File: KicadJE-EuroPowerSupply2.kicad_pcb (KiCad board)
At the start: 2 copper layers, 159 x 128 mm, 148 parts, among them J101 RampOut1, J102 PulseOut2, J103 SawOut3, J104 In1.1, J105 In1.2, J106 In1.3, J107 SS_In2, J108 HS_In3, J109 FM_In4, J110 PWM_In5, J111 SineOut4, P101 HEADER_2x5_Doepfer, Q101 MMBT3906, Q102 UMX1N, SW101 Octave (3 state), U101 TL072, U102 TL072, U103 TL072, U104 AS3340, U105 L78L05_SOT89, U106 L79L05_SOT89, U107 TL072

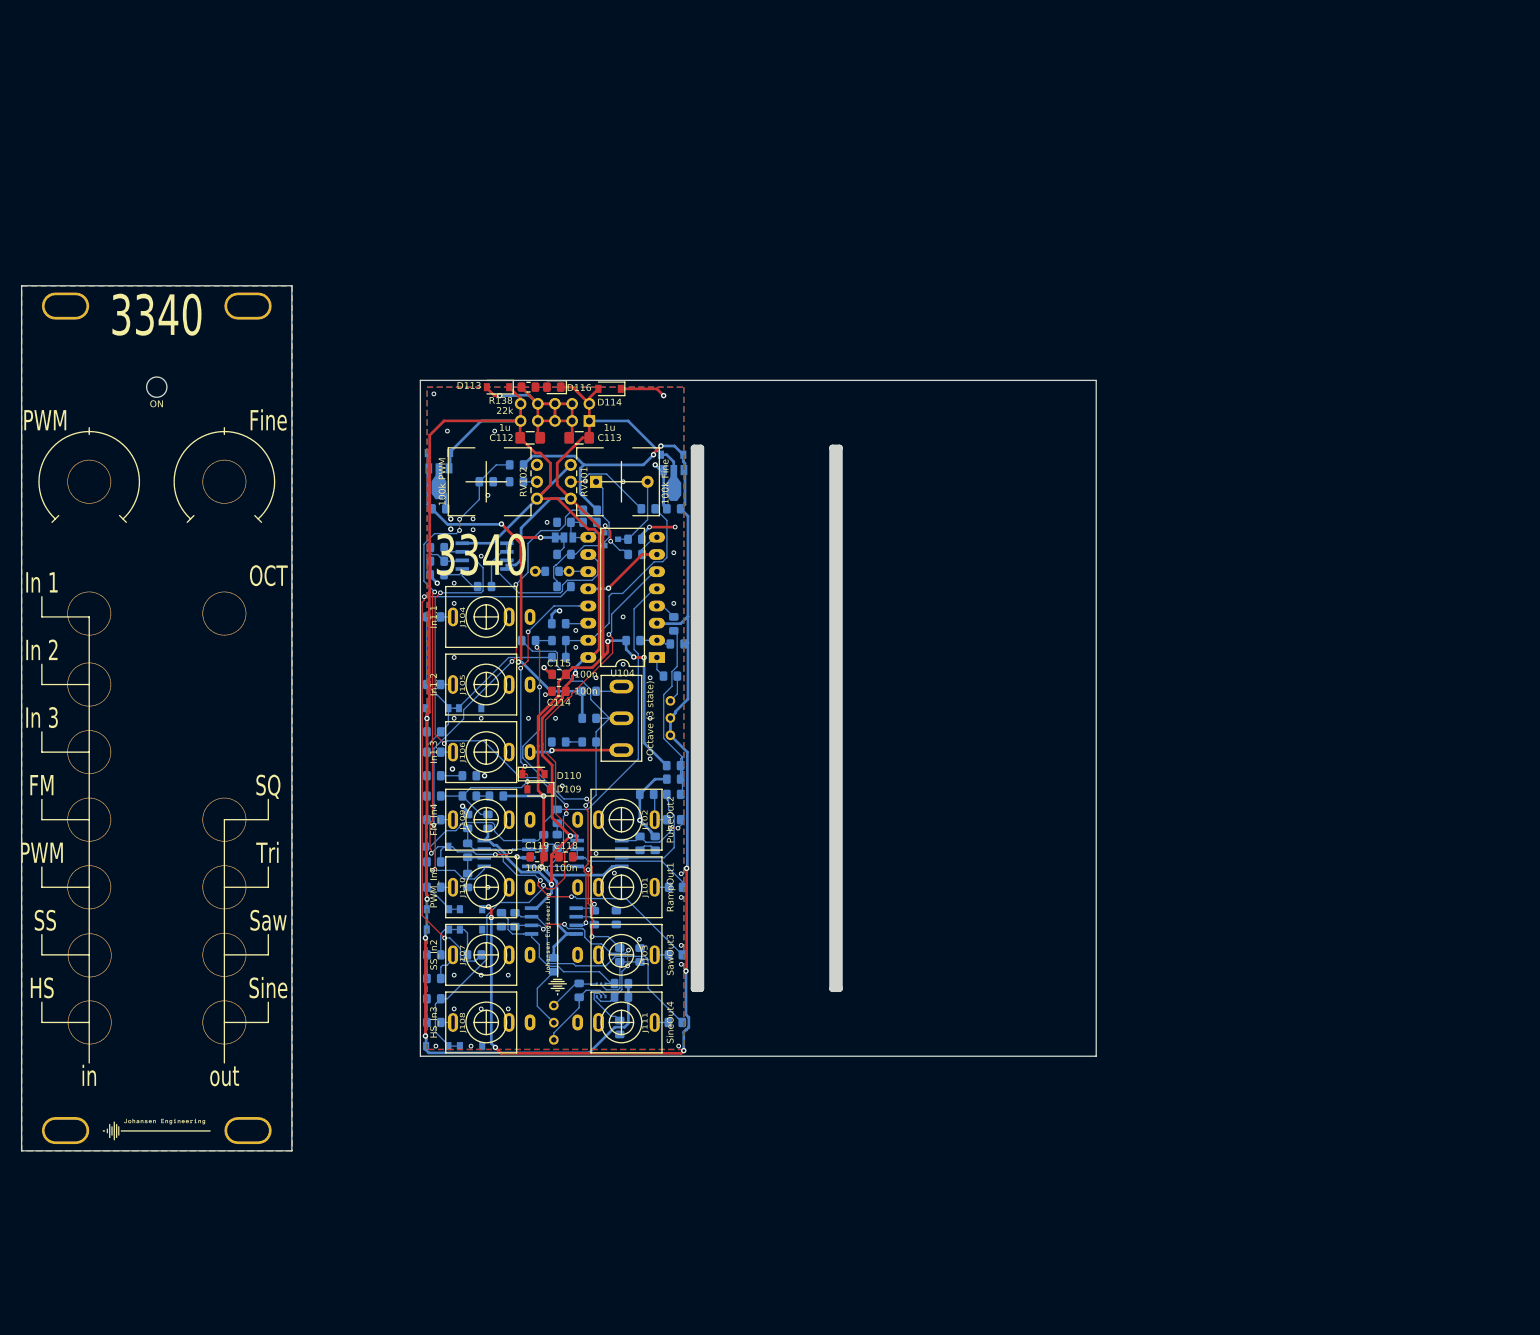
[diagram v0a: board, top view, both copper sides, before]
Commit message: placing first components
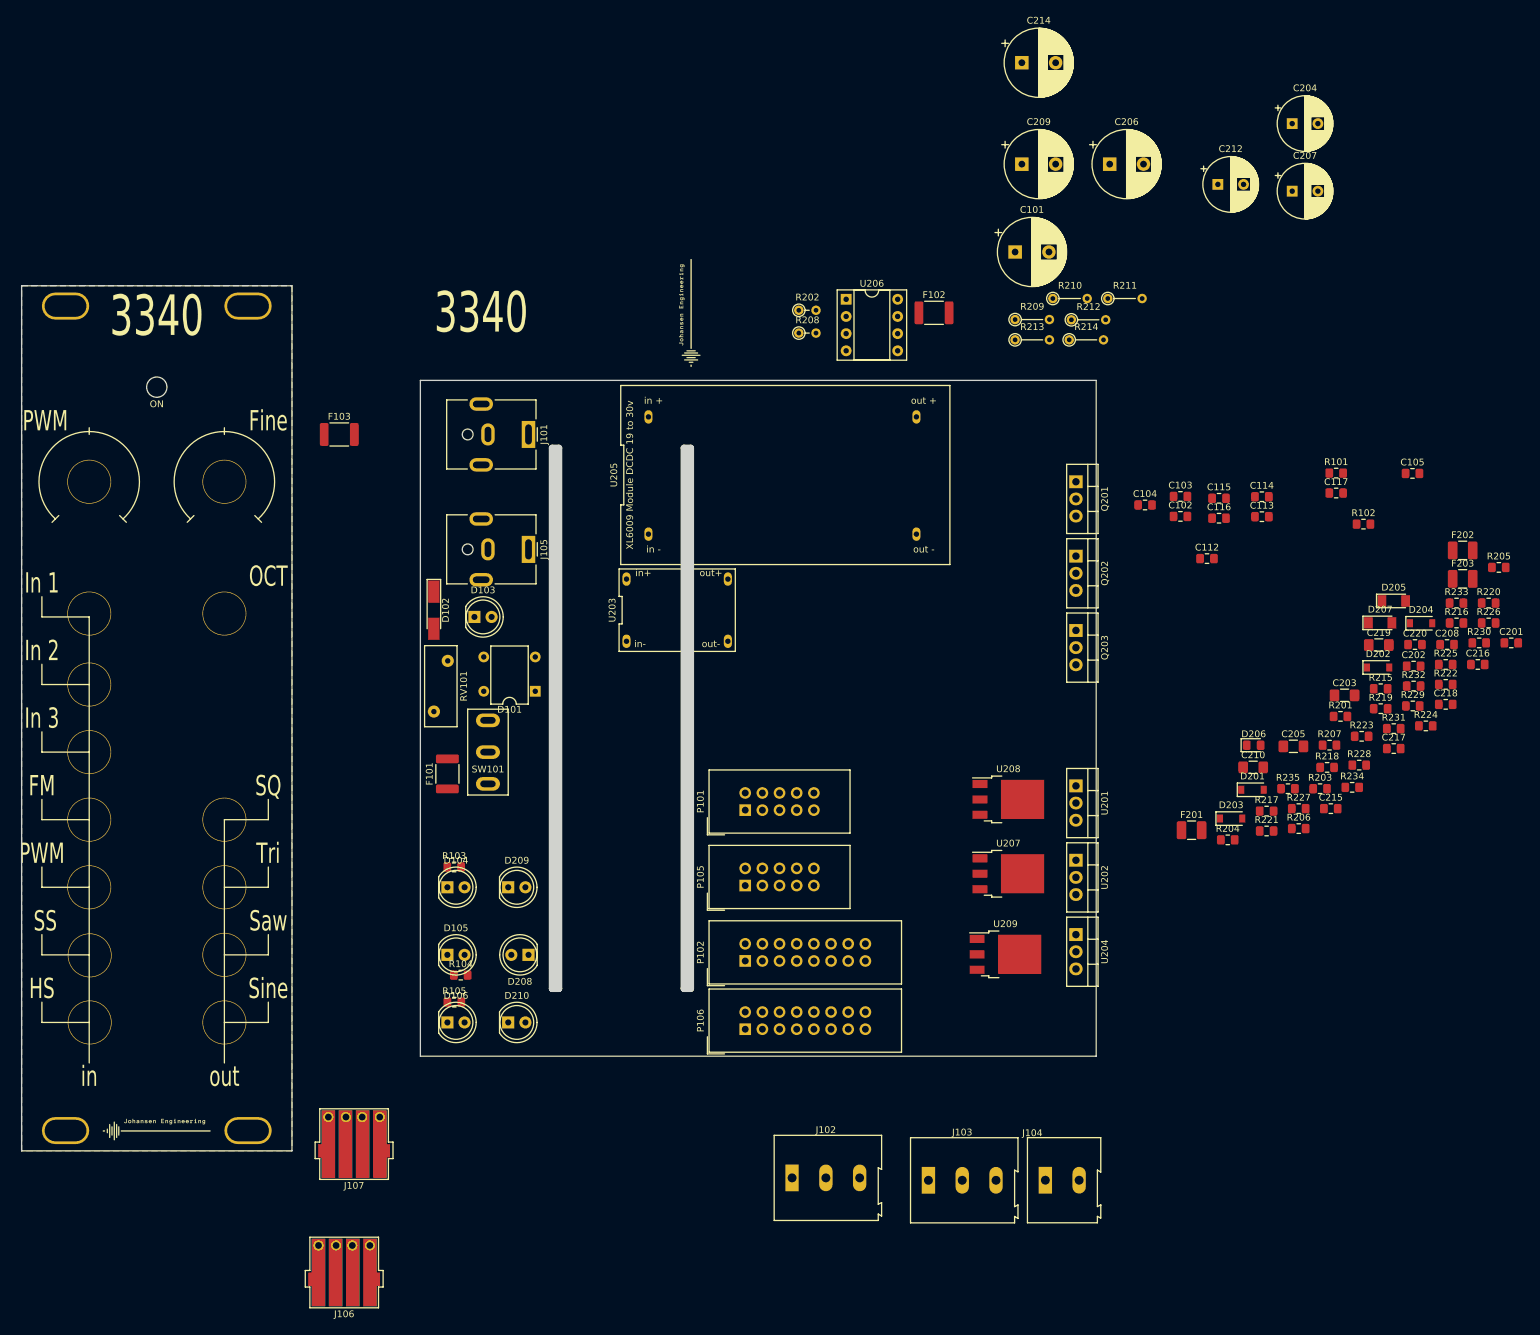
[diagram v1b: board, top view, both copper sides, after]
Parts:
- removed C106: 10n, Capacitor_SMD:C_0805_2012Metric_Pad1.15x1.40mm_HandSolder
- removed C107: 220p, Capacitor_SMD:C_0805_2012Metric_Pad1.15x1.40mm_HandSolder
- removed C108, C109, C118, C119: 100n, Capacitor_SMD:C_0805_2012Metric_Pad1.15x1.40mm_HandSolder
- removed C110: 1n poly, Capacitor_THT:C_Rect_L7.0mm_W2.0mm_P5.00mm
- removed C111: 1n alt, Capacitor_SMD:C_0805_2012Metric_Pad1.15x1.40mm_HandSolder
- removed D107, D108, D109, D110, D113, D114, D117, D118: 1N1007, Diode_SMD:D_SOD-123
- removed D112: 1N4148, Diode_SMD:D_SOD-123
- removed D115: Germanium, Diode_THT:D_A-405_P7.62mm_Horizontal
- removed D116: LED, LED_SMD:LED_0805_2012Metric_Pad1.15x1.40mm_HandSolder
- removed J108: HS_In3, AJ-Dropbox-Kicad:PJ301SM
- removed J109: FM_In4, AJ-Dropbox-Kicad:PJ301SM
- removed J110: PWM_In5, AJ-Dropbox-Kicad:PJ301SM
- removed J111: SineOut4, AJ-Dropbox-Kicad:PJ301SM
- removed JP101: Jumper, Jumper:SolderJumper-3_P1.3mm_Bridged12_Pad1.0x1.5mm_NumberLabels
- removed Q101: MMBT3906, Package_TO_SOT_SMD:SOT-23
- removed Q102: UMX1N, AJ:UMX1N_UMT6_DualNPN
- removed R106: 910R, Resistor_SMD:R_0805_2012Metric_Pad1.15x1.40mm_HandSolder
- removed R107, R111, R112, R113, R116, R153, R155, R164: 1k, Resistor_SMD:R_0805_2012Metric_Pad1.15x1.40mm_HandSolder
- removed R108, R109, R110, R120, R122, R123, R124, R132, R133, R156: 100k, Resistor_SMD:R_0805_2012Metric_Pad1.15x1.40mm_HandSolder
- removed R114: 1k6, Resistor_SMD:R_0805_2012Metric_Pad1.15x1.40mm_HandSolder
- removed R115, R119: 1M, Resistor_SMD:R_0805_2012Metric_Pad1.15x1.40mm_HandSolder
- removed R117: 360k, Resistor_SMD:R_0805_2012Metric_Pad1.15x1.40mm_HandSolder
- removed R118, R125: 470R, Resistor_SMD:R_0805_2012Metric_Pad1.15x1.40mm_HandSolder
- removed R121, R128: 12k5, Resistor_SMD:R_0805_2012Metric_Pad1.15x1.40mm_HandSolder
- removed R126, R127, R130, R131, R134, R140, R143, R158, R159, R161: 10k, Resistor_SMD:R_0805_2012Metric_Pad1.15x1.40mm_HandSolder
- removed R129: 1M5, Resistor_SMD:R_0805_2012Metric_Pad1.15x1.40mm_HandSolder
- removed R135, R136, R137: 47k, Resistor_SMD:R_0805_2012Metric_Pad1.15x1.40mm_HandSolder
- removed R138: 22k, Resistor_SMD:R_0805_2012Metric_Pad1.15x1.40mm_HandSolder
- removed R139, R147: 2k20, Resistor_SMD:R_0805_2012Metric_Pad1.15x1.40mm_HandSolder
- removed R141: 390R, Resistor_SMD:R_0805_2012Metric_Pad1.15x1.40mm_HandSolder
- removed R142: 18k, Resistor_SMD:R_0805_2012Metric_Pad1.15x1.40mm_HandSolder
- removed R144: 26k7, Resistor_SMD:R_0805_2012Metric_Pad1.15x1.40mm_HandSolder
- removed R145: 6k04, Resistor_SMD:R_0805_2012Metric_Pad1.15x1.40mm_HandSolder
- removed R146: 1M2, Resistor_SMD:R_0805_2012Metric_Pad1.15x1.40mm_HandSolder
- removed R148: 1k82, Resistor_SMD:R_0805_2012Metric_Pad1.15x1.40mm_HandSolder
- removed R149, R150: 13k3, Resistor_SMD:R_0805_2012Metric_Pad1.15x1.40mm_HandSolder
- removed R151, R163: OPEN, Resistor_SMD:R_0805_2012Metric_Pad1.15x1.40mm_HandSolder
- removed R152: 0R, Resistor_SMD:R_0805_2012Metric_Pad1.15x1.40mm_HandSolder
- removed R154: 3k, Resistor_SMD:R_0805_2012Metric_Pad1.15x1.40mm_HandSolder
- removed R157: 15k, Resistor_SMD:R_0805_2012Metric_Pad1.15x1.40mm_HandSolder
- removed R160, R162: 25k, Resistor_SMD:R_0805_2012Metric_Pad1.15x1.40mm_HandSolder
- removed RV102: 100k PWM, AJ-Dropbox-Kicad:Potentiometer_China_RK09_Single_Vertical_AJ
- removed RV103: 5k, Potentiometer_THT:Potentiometer_Bourns_3296W_Vertical
- removed RV104: 50k, Potentiometer_THT:Potentiometer_Bourns_3296W_Vertical
- removed U101, U102, U103, U107: TL072, AJ-Dropbox-Kicad:AJ_SO-8_5.3x6.2mm_P1.27mm
- removed U104: AS3340, Package_DIP:DIP-16_W10.16mm_LongPads
- removed U105: L78L05_SOT89, Package_TO_SOT_SMD:SOT-89-3
- removed U106: L79L05_SOT89, Package_TO_SOT_SMD:SOT-89-3
- added C201: 100n, Capacitor_SMD:C_0805_2012Metric_Pad1.15x1.40mm_HandSolder, F.Cu at (211.4, 88.8)
- added C202: 100n, Capacitor_SMD:C_0805_2012Metric_Pad1.15x1.40mm_HandSolder, F.Cu at (197.0, 92.3)
- added C203: 1u, Capacitor_SMD:C_1206_3216Metric_Pad1.42x1.75mm_HandSolder, F.Cu at (186.7, 96.6)
- added C204: 1000uF, Capacitor_THT:CP_Radial_D8.0mm_P3.80mm, F.Cu at (179.0, 12.0)
- added C205: 1u, Capacitor_SMD:C_1206_3216Metric_Pad1.42x1.75mm_HandSolder, F.Cu at (179.2, 104.1)
- added C206: 1000uF, Capacitor_THT:CP_Radial_D10.0mm_P5.00mm, F.Cu at (152.0, 18.0)
- added C207: 1000uF, Capacitor_THT:CP_Radial_D8.0mm_P3.80mm, F.Cu at (179.0, 22.0)
- added C208: 100n, Capacitor_SMD:C_0805_2012Metric_Pad1.15x1.40mm_HandSolder, F.Cu at (201.9, 89.1)
- added C209: 1000uF, Capacitor_THT:CP_Radial_D10.0mm_P5.00mm, F.Cu at (139.0, 18.0)
- added C210: 1u, Capacitor_SMD:C_1206_3216Metric_Pad1.42x1.75mm_HandSolder, F.Cu at (173.2, 107.3)
- added C212: 1000uF, Capacitor_THT:CP_Radial_D8.0mm_P3.80mm, F.Cu at (168.0, 21.0)
- added C214: 1000uF, Capacitor_THT:CP_Radial_D10.0mm_P5.00mm, F.Cu at (139.0, 3.00)
- added C215: 100n, Capacitor_SMD:C_0805_2012Metric_Pad1.15x1.40mm_HandSolder, F.Cu at (184.7, 113.4)
- added C216: 220n, Capacitor_SMD:C_0805_2012Metric_Pad1.15x1.40mm_HandSolder, F.Cu at (206.5, 92.0)
- added C217: 220n, Capacitor_SMD:C_0805_2012Metric_Pad1.15x1.40mm_HandSolder, F.Cu at (194.0, 104.5)
- added C218: 220n, Capacitor_SMD:C_0805_2012Metric_Pad1.15x1.40mm_HandSolder, F.Cu at (201.7, 97.9)
- added C219: 1u, Capacitor_SMD:C_1206_3216Metric_Pad1.42x1.75mm_HandSolder, F.Cu at (191.8, 89.2)
- added C220: 220n, Capacitor_SMD:C_0805_2012Metric_Pad1.15x1.40mm_HandSolder, F.Cu at (197.2, 89.1)
- added D201: 1N4001, Diode_SMD:D_SOD-123, F.Cu at (173.1, 110.6)
- added D202: 1N4001, Diode_SMD:D_SOD-123, F.Cu at (191.7, 92.5)
- added D203: 1N4001, Diode_SMD:D_SOD-123, F.Cu at (170.0, 114.8)
- added D204: 1N4001, Diode_SMD:D_SOD-123, F.Cu at (198.1, 85.9)
- added D205: 15v, Diode_SMD:D_MiniMELF, F.Cu at (194.0, 82.6)
- added D206: LED, LED_SMD:LED_0805_2012Metric_Pad1.15x1.40mm_HandSolder, F.Cu at (173.3, 104.0)
- added D207: 15v, Diode_SMD:D_MiniMELF, F.Cu at (192.0, 85.9)
- added D208: RED, LED_THT:LED_D5.0mm, F.Cu at (66.0, 135.0)
- added D209: RED, LED_THT:LED_D5.0mm, F.Cu at (63.0, 125.0)
- added D210: RED, LED_THT:LED_D5.0mm, F.Cu at (63.0, 145.0)
- added F101: 750mA, Fuse:Fuse_1812_4532Metric_Pad1.30x3.40mm_HandSolder, F.Cu at (54.0, 108.2)
- added F102: 750mA, Fuse:Fuse_1812_4532Metric_Pad1.30x3.40mm_HandSolder, F.Cu at (126.0, 40.0)
- added F103: 750mA, Fuse:Fuse_1812_4532Metric_Pad1.30x3.40mm_HandSolder, F.Cu at (38.0, 58.0)
- added F201: 750mA, Fuse:Fuse_1210_3225Metric_Pad1.42x2.65mm_HandSolder, F.Cu at (164.1, 116.6)
- added F202: 750mA, Fuse:Fuse_1210_3225Metric_Pad1.42x2.65mm_HandSolder, F.Cu at (204.2, 75.2)
- added F203: 750mA, Fuse:Fuse_1210_3225Metric_Pad1.42x2.65mm_HandSolder, F.Cu at (204.2, 79.4)
- added P102: Doepfer_Power_16pin, Connectors_IDC:IDC-Header_2x08_Pitch2.54mm_Straight, F.Cu at (98.1, 135.9)
- added P105: Doepfer_Power_10pin, Connectors_IDC:IDC-Header_2x05_Pitch2.54mm_Straight, F.Cu at (98.1, 124.7)
- added P106: Doepfer_Power_16pin, Connectors_IDC:IDC-Header_2x08_Pitch2.54mm_Straight, F.Cu at (98.1, 146.0)
- added Q201: TIP41, Package_TO_SOT_THT:TO-220-3_Vertical, F.Cu at (147.0, 65.0)
- added Q202: TIP41, Package_TO_SOT_THT:TO-220-3_Vertical, F.Cu at (147.0, 76.0)
- added Q203: TIP42, Package_TO_SOT_THT:TO-220-3_Vertical, F.Cu at (147.0, 87.0)
- added R201: 0R, Resistor_SMD:R_0805_2012Metric_Pad1.15x1.40mm_HandSolder, F.Cu at (186.1, 99.7)
- added R202: 10r, Resistor_THT:R_Axial_DIN0204_L3.6mm_D1.6mm_P2.54mm_Vertical, F.Cu at (106.0, 39.6)
- added R203: 100r, Resistor_SMD:R_0805_2012Metric_Pad1.15x1.40mm_HandSolder, F.Cu at (183.1, 110.4)
- added R204: 4k70, Resistor_SMD:R_0805_2012Metric_Pad1.15x1.40mm_HandSolder, F.Cu at (169.5, 118.0)
- added R205: 10k, Resistor_SMD:R_0805_2012Metric_Pad1.15x1.40mm_HandSolder, F.Cu at (209.6, 77.7)
- added R206: 330r, Resistor_SMD:R_0805_2012Metric_Pad1.15x1.40mm_HandSolder, F.Cu at (180.0, 116.3)
- added R207: 4k70, Resistor_SMD:R_0805_2012Metric_Pad1.15x1.40mm_HandSolder, F.Cu at (184.5, 104.0)
- added R208: 10r, Resistor_THT:R_Axial_DIN0204_L3.6mm_D1.6mm_P2.54mm_Vertical, F.Cu at (106.0, 43.0)
- added R209: 0r25, Resistor_THT:R_Axial_DIN0204_L3.6mm_D1.6mm_P5.08mm_Vertical, F.Cu at (138.0, 41.0)
- added R210: 0r25, Resistor_THT:R_Axial_DIN0204_L3.6mm_D1.6mm_P5.08mm_Vertical, F.Cu at (143.6, 37.9)
- added R211: 0r25, Resistor_THT:R_Axial_DIN0204_L3.6mm_D1.6mm_P5.08mm_Vertical, F.Cu at (151.7, 37.9)
- added R212: 0r25, Resistor_THT:R_Axial_DIN0204_L3.6mm_D1.6mm_P5.08mm_Vertical, F.Cu at (146.3, 41.0)
- added R213: 0r25, Resistor_THT:R_Axial_DIN0204_L3.6mm_D1.6mm_P5.08mm_Vertical, F.Cu at (138.0, 44.0)
- added R214: 0r25, Resistor_THT:R_Axial_DIN0204_L3.6mm_D1.6mm_P5.08mm_Vertical, F.Cu at (146.0, 44.0)
- added R215: 1k, Resistor_SMD:R_0805_2012Metric_Pad1.15x1.40mm_HandSolder, F.Cu at (192.1, 95.6)
- added R216: 1k, Resistor_SMD:R_0805_2012Metric_Pad1.15x1.40mm_HandSolder, F.Cu at (203.3, 85.9)
- added R217: 1R1, Resistor_SMD:R_0805_2012Metric_Pad1.15x1.40mm_HandSolder, F.Cu at (175.2, 113.7)
- added R218: 1R1, Resistor_SMD:R_0805_2012Metric_Pad1.15x1.40mm_HandSolder, F.Cu at (184.2, 107.3)
- added R219: 1R1, Resistor_SMD:R_0805_2012Metric_Pad1.15x1.40mm_HandSolder, F.Cu at (192.1, 98.6)
- added R220: 1R1, Resistor_SMD:R_0805_2012Metric_Pad1.15x1.40mm_HandSolder, F.Cu at (208.1, 82.9)
- added R221: 5k6, Resistor_SMD:R_0805_2012Metric_Pad1.15x1.40mm_HandSolder, F.Cu at (175.2, 116.7)
- added R222: 100k, Resistor_SMD:R_0805_2012Metric_Pad1.15x1.40mm_HandSolder, F.Cu at (201.7, 95.0)
- added R223: 100k, Resistor_SMD:R_0805_2012Metric_Pad1.15x1.40mm_HandSolder, F.Cu at (189.3, 102.7)
- added R224: 4k7, Resistor_SMD:R_0805_2012Metric_Pad1.15x1.40mm_HandSolder, F.Cu at (198.8, 101.1)
- added R225: 1R1, Resistor_SMD:R_0805_2012Metric_Pad1.15x1.40mm_HandSolder, F.Cu at (201.7, 92.0)
- added R226: 1R1, Resistor_SMD:R_0805_2012Metric_Pad1.15x1.40mm_HandSolder, F.Cu at (208.1, 85.9)
- added R227: 1R1, Resistor_SMD:R_0805_2012Metric_Pad1.15x1.40mm_HandSolder, F.Cu at (180.0, 113.4)
- added R228: 1R1, Resistor_SMD:R_0805_2012Metric_Pad1.15x1.40mm_HandSolder, F.Cu at (188.9, 106.9)
- added R229: 1R1, Resistor_SMD:R_0805_2012Metric_Pad1.15x1.40mm_HandSolder, F.Cu at (196.8, 98.2)
- added R230: 1R1, Resistor_SMD:R_0805_2012Metric_Pad1.15x1.40mm_HandSolder, F.Cu at (206.7, 88.8)
- added R231: 1R1, Resistor_SMD:R_0805_2012Metric_Pad1.15x1.40mm_HandSolder, F.Cu at (194.0, 101.5)
- added R232: 1R1, Resistor_SMD:R_0805_2012Metric_Pad1.15x1.40mm_HandSolder, F.Cu at (197.0, 95.2)
- added R233: 1k, Resistor_SMD:R_0805_2012Metric_Pad1.15x1.40mm_HandSolder, F.Cu at (203.3, 82.9)
- added R234: 15k, Resistor_SMD:R_0805_2012Metric_Pad1.15x1.40mm_HandSolder, F.Cu at (187.9, 110.2)
- added R235: 100k, Resistor_SMD:R_0805_2012Metric_Pad1.15x1.40mm_HandSolder, F.Cu at (178.4, 110.4)
- added U201: LM7812_TO220, Package_TO_SOT_THT:TO-220-3_Vertical, F.Cu at (147.0, 110.0)
- added U202: LM7805_TO220, Package_TO_SOT_THT:TO-220-3_Vertical, F.Cu at (147.0, 121.0)
- added U203: Step Down Module +15 to 7v - MP2307, AJ:MP2307 DCDC module, F.Cu at (88.0, 84.0)
- added U204: LM7912_TO220, Package_TO_SOT_THT:TO-220-3_Vertical, F.Cu at (147.0, 132.0)
- added U205: XL6009 Module DCDC 19 to 30v, AJ:XL6009-DCDC-Module, F.Cu at (104.0, 64.0)
- added U206: TL071, Package_DIP:DIP-8_W7.62mm_Socket, F.Cu at (113.0, 38.0)
- added U207: LM78M05_TO252, Package_TO_SOT_SMD:TO-252-3_TabPin2, F.Cu at (137.0, 123.0)
- added U208: LM78M12_TO252, Package_TO_SOT_SMD:TO-252-3_TabPin2, F.Cu at (137.0, 112.0)
- added U209: MC79M12_TO252, Package_TO_SOT_SMD:TO-252-3_TabPin2, F.Cu at (136.6, 134.9)
- C101: value 100n -> 100uF; footprint Capacitor_SMD:C_0805_2012Metric_Pad1.15x1.40mm_HandSolder -> Capacitor_THT:CP_Radial_D10.0mm_P5.00mm; moved to F.Cu
- C102, C103: value 1n -> 100n; moved to F.Cu
- C104, C105: value 10n -> 100n; moved to F.Cu
- C112, C113: value 1u -> 100n; footprint Capacitor_SMD:C_1206_3216Metric_Pad1.42x1.75mm_HandSolder -> Capacitor_SMD:C_0805_2012Metric_Pad1.15x1.40mm_HandSolder
- C116, C117: moved to F.Cu
- D101: value 1N1007 -> B125C800DM - DB107; footprint Diode_SMD:D_SOD-123 -> Diode_THT:Diode_Bridge_DIP-4_W7.62mm_P5.08mm; moved to F.Cu
- D102: value 1N1007 -> 27v; footprint Diode_SMD:D_SOD-123 -> Diode_SMD:D_MiniMELF_Handsoldering; moved to F.Cu
- D103: value 1N1007 -> PWR_IN_LED; footprint Diode_SMD:D_SOD-123 -> LED_THT:LED_D5.0mm; moved to F.Cu
- D104, D105, D106: value 1N1007 -> LED; footprint Diode_SMD:D_SOD-123 -> LED_THT:LED_D5.0mm; moved to F.Cu
- J101: value RampOut1 -> Laptop Power; footprint AJ-Dropbox-Kicad:PJ301SM -> Connector_BarrelJack:BarrelJack_CUI_PJ-063AH_Horizontal
- J102: value PulseOut2 -> +-15V thru; footprint AJ-Dropbox-Kicad:PJ301SM -> TerminalBlock:TerminalBlock_Altech_AK300-3_P5.00mm
- J103: value SawOut3 -> +-12v out; footprint AJ-Dropbox-Kicad:PJ301SM -> TerminalBlock:TerminalBlock_Altech_AK300-3_P5.00mm
- J104: value In1.1 -> +5V out; footprint AJ-Dropbox-Kicad:PJ301SM -> TerminalBlock:TerminalBlock_Altech_AK300-2_P5.00mm
- J105: value In1.2 -> Laptop Power Out; footprint AJ-Dropbox-Kicad:PJ301SM -> Connector_BarrelJack:BarrelJack_CUI_PJ-063AH_Horizontal
- J106: value In1.3 -> FrontInterConnVin; footprint AJ-Dropbox-Kicad:PJ301SM -> AJ-Dropbox-Kicad:BoardConnector2x2.54x10mm4pin
- J107: value SS_In2 -> BaseInterConnVin; footprint AJ-Dropbox-Kicad:PJ301SM -> AJ-Dropbox-Kicad:BoardConnector2x2.54x10mm4pin
- P101: value HEADER_2x5_Doepfer -> Doepfer_Power_10pin; footprint Connector_IDC:IDC-Header_2x05_P2.54mm_Vertical -> Connectors_IDC:IDC-Header_2x05_Pitch2.54mm_Straight; moved to F.Cu
- R101: value 47k -> 10r; moved to F.Cu
- R102: value 470R -> 10k; moved to F.Cu
- R103: value 82k -> 4k7; moved to F.Cu
- R104: value 20k -> 1k5; moved to F.Cu
- R105: value 1k -> 4k7; moved to F.Cu
- RV101: value 100k Fine -> Varistor; footprint AJ-Dropbox-Kicad:Potentiometer_China_RK09_Single_Vertical_AJ -> Varistor:RV_Disc_D12mm_W4.8mm_P7.5mm
- SW101: value Octave (3 state) -> SW_SPDT
- moved C105 143.7 mm to (196.8, 63.8), turned to 0 degrees
- moved C103 133.1 mm to (162.5, 67.2), turned to 0 degrees
- moved C102 128.1 mm to (162.5, 70.1), turned to 0 degrees
- moved R102 123.4 mm to (189.5, 71.3), turned to 0 degrees
- moved C101 120.2 mm to (138.0, 31.0)
- moved J104 117.4 mm to (142.5, 168.3), turned to 0 degrees
- moved C116 115.4 mm to (168.2, 70.4), turned to 0 degrees
- moved R101 115.1 mm to (185.5, 63.7), turned to 0 degrees
- moved C114 107.9 mm to (174.5, 67.2), turned to 0 degrees
- moved C104 107.7 mm to (157.2, 68.4), turned to 0 degrees
- moved C112 101.7 mm to (166.4, 76.4)
- moved C113 101.7 mm to (174.5, 70.2)
- moved C115 101.1 mm to (168.2, 67.4)
- moved C117 98.0 mm to (185.5, 66.7)
- moved G*** 95.1 mm to (90.0, 40.0)
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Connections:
- C101 pad 1: Net-(C101-Pad1) -> Vin-Pos19
- C101 pad 2: Net-(C101-Pad2) -> Vin-Neg19
- C102 pad 1: 3SoftSyncIn2 -> GND
- C102 pad 2: Net-(C102-Pad2) -> +12V
- C103 pad 1: 3HardSyncIn3 -> GND
- C103 pad 2: Net-(C103-Pad2) -> +12V
- C104 pad 2: Net-(C104-Pad2) -> +12V
- C105 pad 1: -12VA -> GND
- C105 pad 2: Net-(C105-Pad2) -> +12V
- C112 pad 1: +12VA -> +5V
- C113 pad 1: GND -> +5V
- C113 pad 2: -12VA -> GND
- C114 pad 1: +12VA -> -12V
- C115 pad 1: GND -> -12V
- C115 pad 2: -12VA -> GND
- C116 pad 1: GND -> -12V
- C116 pad 2: +5V -> GND
- C117 pad 1: GND -> -12V
- C117 pad 2: -5V -> GND
- D101 pad 1: +12VA -> Vin-Pos19
- D101 pad 2: Net-(D101-Pad2) -> Vin-Neg19
- D102 pad 1: Net-(D101-Pad2) -> Net-(D102-Pad1)
- D102 pad 2: -5V -> /DCSleeve
- D103 pad 1: +12VA -> Vin-Neg19
- D104 pad 1: Net-(D103-Pad2) -> Net-(D104-Pad1)
- D104 pad 2: GND -> +12V
- D105 pad 1: +12VA -> GND
- D105 pad 2: 3SoftSyncIn2 -> Net-(D105-Pad2)
- D106 pad 1: +12VA -> Net-(D106-Pad1)
- D106 pad 2: 3HardSyncIn3 -> GND
- P101 pad 1: -12VA -> -12V
- P101 pad 10: +12VA -> +12V
- P101 pad 2: -12VA -> -12V
- P101 pad 9: +12VA -> +12V
- R101 pad 1: Net-(R101-Pad1) -> Net-(D101-Pad4)
- R101 pad 2: +5V -> Net-(D102-Pad1)
- R102 pad 1: Net-(R102-Pad1) -> Vin-Pos19
- R102 pad 2: GND -> Net-(D103-Pad2)
- R103 pad 1: 3Octave -> GND
- R103 pad 2: +5V -> Net-(D104-Pad1)
- R104 pad 1: Net-(R102-Pad1) -> +5V
- R104 pad 2: 3Octave -> Net-(D105-Pad2)
- R105 pad 1: Net-(R105-Pad1) -> -12V
- R105 pad 2: Net-(J101-PadT) -> Net-(D106-Pad1)
- RV101 pad 1: -12VA -> Net-(D101-Pad4)
- RV101 pad 2: Net-(R119-Pad1) -> /DCSleeve
- SW101 pad 1: GND -> Net-(F101-Pad1)
- SW101 pad 2: 3Octave -> Net-(J101-Pad1)
- SW101 pad 3: Net-(R101-Pad1) -> (no net)
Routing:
- net +12VA: track 297.1 -> 0.00 mm, vias 7 -> 0
- net -12VA: track 193.5 -> 0.00 mm, vias 5 -> 0
- net -5V: track 182.7 -> 0.00 mm, vias 8 -> 0
- net GND: track 110.0 -> 0.00 mm, vias 60 -> 0
- net 3HardSyncIn3: track 95.7 -> 0.00 mm, vias 2 -> 0
- net 3VTO_1: track 93.2 -> 0.00 mm, vias 6 -> 0
- net Net-(C106-Pad1): track 90.3 -> 0.00 mm, vias 6 -> 0
- net Net-(C107-Pad1): track 82.3 -> 0.00 mm, vias 2 -> 0
- net Net-(R127-Pad2): track 77.2 -> 0.00 mm, vias 4 -> 0
- net 3PWM_In5: track 67.7 -> 0.00 mm
- net +5V: track 62.7 -> 0.00 mm, vias 3 -> 0
- net 3Octave: track 59.1 -> 0.00 mm, vias 2 -> 0
- net 3FM_Lin_In4: track 54.0 -> 0.00 mm, vias 4 -> 0
- net Net-(R151-Pad1): track 52.1 -> 0.00 mm, vias 4 -> 0
- net Net-(D103-Pad2): track 44.7 -> 0.00 mm
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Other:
- outline, holes or cut-outs redrawn

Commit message: Faceplate
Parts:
- removed H103, H104: MountingHole_Pad, AJ:MountingHole_Eurorack3
- removed TP101: Oct, AJ:Pot_6m3
- removed TP102: In1, AJ:Jack_6m3
- removed TP103: In2, AJ:Jack_6m3
- removed TP104: In3, AJ:Jack_6m3
- removed TP105: SS, AJ:Jack_6m3
- removed TP106: HS, AJ:Jack_6m3
- removed TP107: FM, AJ:Jack_6m3
- removed TP108: PWM, AJ:Jack_6m3
- removed TP111: Saw, AJ:Jack_6m3
- removed TP112: Fine, AJ:Pot_6m3_scale1
- removed TP113: PWM, AJ:Pot_6m3_scale1
- removed TP115: 3m5 jack, AJ:Jack_6m3
- added H105: OL, AJ:LED_Hole_3mm, F.Cu at (6.00, 145.0)
- added H105: ON, AJ:LED_Hole_3mm, F.Cu at (-4.00, 145.0)
- added H105: OL, AJ:LED_Hole_3mm, F.Cu at (6.00, 135.0)
- added H105: ON, AJ:LED_Hole_3mm, F.Cu at (-4.00, 135.0)
- added H105: OL, AJ:LED_Hole_3mm, F.Cu at (6.00, 125.0)
- added H105: ON, AJ:LED_Hole_3mm, F.Cu at (-4.00, 125.0)
- added REF**: MountingHole_3.2mm_M3_Pad_Via, MountingHole:MountingHole_3.2mm_M3_Pad_Via, F.Cu at (146.0, 55.0)
- added REF**: MountingHole_3.2mm_M3_Pad_Via, MountingHole:MountingHole_3.2mm_M3_Pad_Via, F.Cu at (146.0, 145.0)
- added REF**: MountingHole_3.2mm_M3_Pad_Via, MountingHole:MountingHole_3.2mm_M3_Pad_Via, F.Cu at (76.0, 145.0)
- added REF**: MountingHole_3.2mm_M3_Pad_Via, MountingHole:MountingHole_3.2mm_M3_Pad_Via, F.Cu at (76.0, 55.0)
- added TP110: SQ, AJ:Jack_6m3, F.Cu at (1.00, 105.0)
- D101, D102, F101, R101, RV101: moved to B.Cu
- moved R101 135.4 mm to (52.0, 86.0), turned to 90 degrees
- moved F103 120.4 mm to (105.0, 158.0), turned to 90 degrees
- moved C101 80.8 mm to (77.0, 84.0)
- moved J106 74.0 mm to (38.0, 108.0)
- moved J107 71.0 mm to (37.8, 92.0)
- moved TP110 40.0 mm to (1.00, 75.0)
- moved H105 35.4 mm to (1.00, 85.0)
- moved TP109 26.0 mm to (1.00, 58.5)
- moved U203 13.0 mm to (101.0, 84.0)
- moved G*** 11.2 mm to (1.00, 156.0)
- moved RV101 7.00 mm to (52.0, 92.0), turned to 270 degrees
- moved D102 6.00 mm to (52.0, 78.0), turned to 90 degrees
- moved D101 4.12 mm to (66.0, 92.0)
- moved F101 3.38 mm to (53.0, 105.0)
- turned SW101 to 180 degrees
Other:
- outline, holes or cut-outs redrawn
- board text added: "+12"
- board text added: "+5"
- board text added: "-12"
- board text added: "In"
- board text added: "Out"
- board text added: "PWR2"
- board text added: "on"
- board text removed: "FM"
- board text removed: "Fine"
- board text removed: "HS"
- board text removed: "In 1"
- board text removed: "In 2"
- board text removed: "In 3"
- board text removed: "OCT"
- board text removed: "PWM"
- board text removed: "SQ"
- board text removed: "SS"
- board text removed: "Saw"
- board text removed: "Sine"
- board text removed: "Tri"
- board text removed: "in"
- board text removed: "out"

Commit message: Update KicadJE-EuroPowerSupply2.kicad_pcb
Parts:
- C102, C103, C104, C105, C112, C113, C114, C115, C116, C117, C201, C202, C203, C205, C208, C210, C215, C216, C217, C218, C219, C220, D201, D202, D203, D204, D205, D207, F102, F103, F201, F202, F203, R102, R103, R104, R105, R201, R203, R204, R206, R207, R215, R216, R217, R218, R219, R220, R221, R222, R223, R224, R225, R226, R227, R228, R229, R230, R231, R232, R233, R234, R235: moved to B.Cu
- moved R222 168.2 mm to (46.0, 158.5), turned to 180 degrees
- moved R224 160.0 mm to (44.0, 141.5), turned to 180 degrees
- moved R223 154.7 mm to (39.5, 141.5)
- moved R233 151.1 mm to (64.5, 142.5)
- moved R216 146.5 mm to (64.5, 132.5)
- moved R102 145.5 mm to (44.5, 83.0)
- moved R234 132.5 mm to (64.5, 158.5)
- moved R221 132.0 mm to (50.0, 158.5)
- moved R215 130.4 mm to (64.5, 122.5)
- moved C214 129.3 mm to (117.5, 130.5), turned to 270 degrees
- moved R235 127.3 mm to (60.5, 158.5), turned to 180 degrees
- moved C204 120.3 mm to (127.0, 120.5), turned to 270 degrees
- moved C212 117.4 mm to (127.0, 131.0), turned to 270 degrees
- moved C117 112.2 mm to (91.5, 128.0), turned to 90 degrees
- moved C114 111.1 mm to (81.5, 128.0), turned to 90 degrees
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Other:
- outline, holes or cut-outs redrawn
- board text added: "Johansen Engineering PWR2 - Rev A 15/03-2020"
- board text removed: "3340"
- board text removed: "AS3340 Rev A - 07/03-2020 Johansen Engineering"
- board text removed: "JE - AS3340 Rev A 07/03-2020"

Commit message: PCB adjustments
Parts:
- added JP201: SolderJumper_3_Bridged12, Jumper:SolderJumper-3_P1.3mm_Bridged12_RoundedPad1.0x1.5mm_NumberLabels, B.Cu at (133.0, 122.0)
- added JP202: SolderJumper_3_Bridged12, Jumper:SolderJumper-3_P1.3mm_Bridged12_RoundedPad1.0x1.5mm_NumberLabels, B.Cu at (133.0, 137.5)
- added Q204: MMBT2907A, Package_TO_SOT_SMD:SOT-23_Handsoldering, B.Cu at (119.0, 182.5)
- added Q205: MMBT2222A, Package_TO_SOT_SMD:SOT-23_Handsoldering, B.Cu at (118.2, 172.7)
- added Q206: MMBT2907A, Package_TO_SOT_SMD:SOT-23_Handsoldering, B.Cu at (124.7, 177.2)
- moved R221 77.1 mm to (127.0, 155.5)
- moved R222 77.1 mm to (123.0, 155.5)
- moved R234 77.1 mm to (141.5, 155.5)
- moved R235 77.1 mm to (137.5, 155.5)
- moved R223 72.9 mm to (111.0, 155.5)
- moved R224 72.9 mm to (115.5, 155.5)
- moved R217 1.50 mm to (133.2, 125.5)
- moved R218 1.50 mm to (133.2, 127.5)
- moved R219 1.50 mm to (133.2, 129.5)
- moved R220 1.50 mm to (133.2, 131.5)
- moved R229 1.50 mm to (133.0, 113.0)
- moved R230 1.50 mm to (133.0, 111.0)
- moved R231 1.50 mm to (133.0, 115.0)
- moved R232 1.50 mm to (133.0, 117.0)
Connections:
- net Net-(Q204-PadB) renamed /VoltageRegulation/b4
- net Net-(Q205-Pad1) renamed /VoltageRegulation/b5
- R215 pad 1: (no net) -> Net-(Q204-Pad3)
- R216 pad 1: (no net) -> Net-(Q205-Pad3)
- R233 pad 1: (no net) -> Net-(Q206-Pad3)

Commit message: Almost completely placed
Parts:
- added J108: Conn_01x08, Connector_PinHeader_2.54mm:PinHeader_1x08_P2.54mm_Vertical, F.Cu at (93.4, 102.2)
- added J109: Conn_01x08, Connector_PinHeader_2.54mm:PinHeader_1x08_P2.54mm_Vertical, B.Cu at (59.5, 125.5)
- J106: footprint AJ-Dropbox-Kicad:BoardConnector2x2.54x10mm4pin -> Connector_PinHeader_2.54mm:PinHeader_1x04_P2.54mm_Vertical
- J107: value BaseInterConnVin -> FrontInterConnVin; footprint AJ-Dropbox-Kicad:BoardConnector2x2.54x10mm4pin -> Connector_PinHeader_2.54mm:PinHeader_1x04_P2.54mm_Vertical; moved to B.Cu
- moved J106 43.5 mm to (73.5, 88.0), turned to 180 degrees
- moved J107 28.5 mm to (66.0, 88.0)
- moved R102 15.0 mm to (59.5, 82.5), turned to 180 degrees
- moved R215 5.03 mm to (64.0, 127.5)
- moved R103 5.00 mm to (55.5, 127.5)
- moved R216 4.52 mm to (64.0, 137.0)
- moved R104 4.50 mm to (55.5, 137.0), turned to 180 degrees
- moved C102 1.77 mm to (81.2, 121.8)
- moved C103 1.77 mm to (91.2, 121.7)
- moved C104 1.77 mm to (110.8, 121.7)
- moved C105 1.77 mm to (101.8, 121.8)
- moved C112 1.77 mm to (101.8, 116.8)
- moved C113 1.77 mm to (110.8, 116.7)
- moved C114 1.77 mm to (81.2, 129.7)
- moved C115 1.77 mm to (101.8, 129.7)
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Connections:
- net Net-(Q204-Pad3) renamed I+12
- net Net-(Q205-Pad3) renamed I-12
- net Net-(Q206-Pad3) renamed I+5
- J106 pad 2: Vin-Neg19 -> Vin-Pos19
- J106 pad 3: (no net) -> Vin-Neg19
- J106 pad 4: (no net) -> Vin-Neg19
- J107 pad 2: Vin-Neg19 -> Vin-Pos19
- J107 pad 3: (no net) -> Vin-Neg19
- J107 pad 4: (no net) -> Vin-Neg19
